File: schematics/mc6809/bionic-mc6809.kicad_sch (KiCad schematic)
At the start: 5 parts, among them J1 BionicConnector, U1 MC6809P, U2 74HCT126

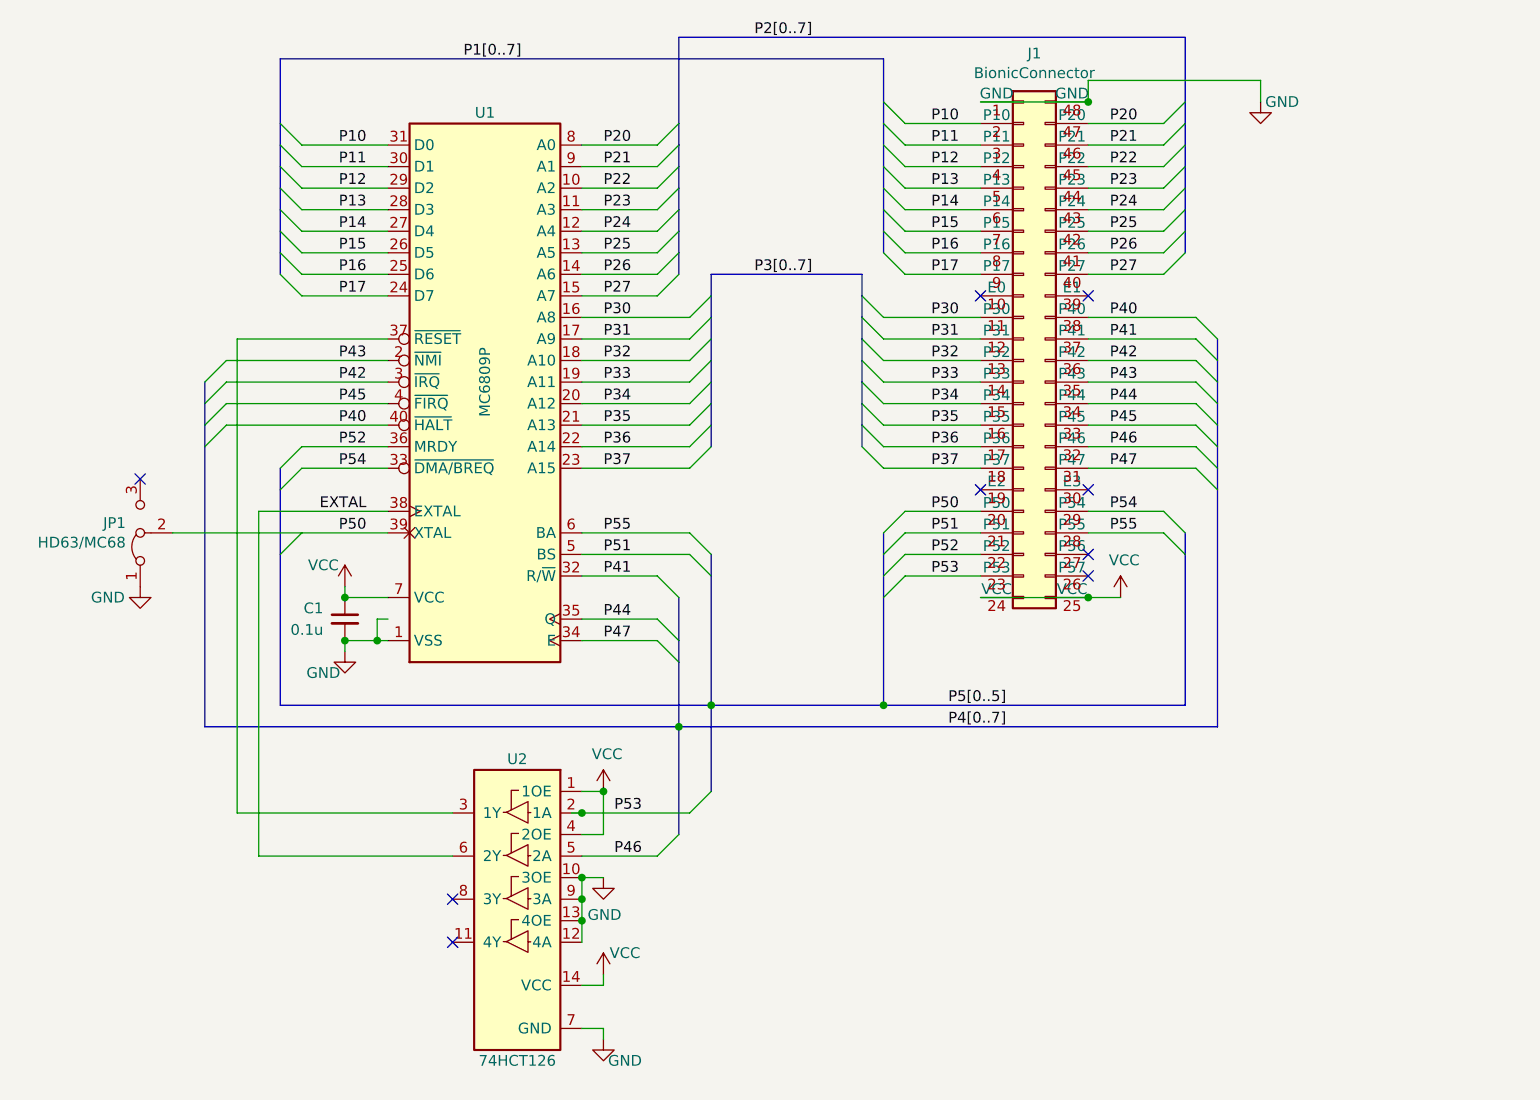
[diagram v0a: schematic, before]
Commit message: [MC6809] Move schematics directory
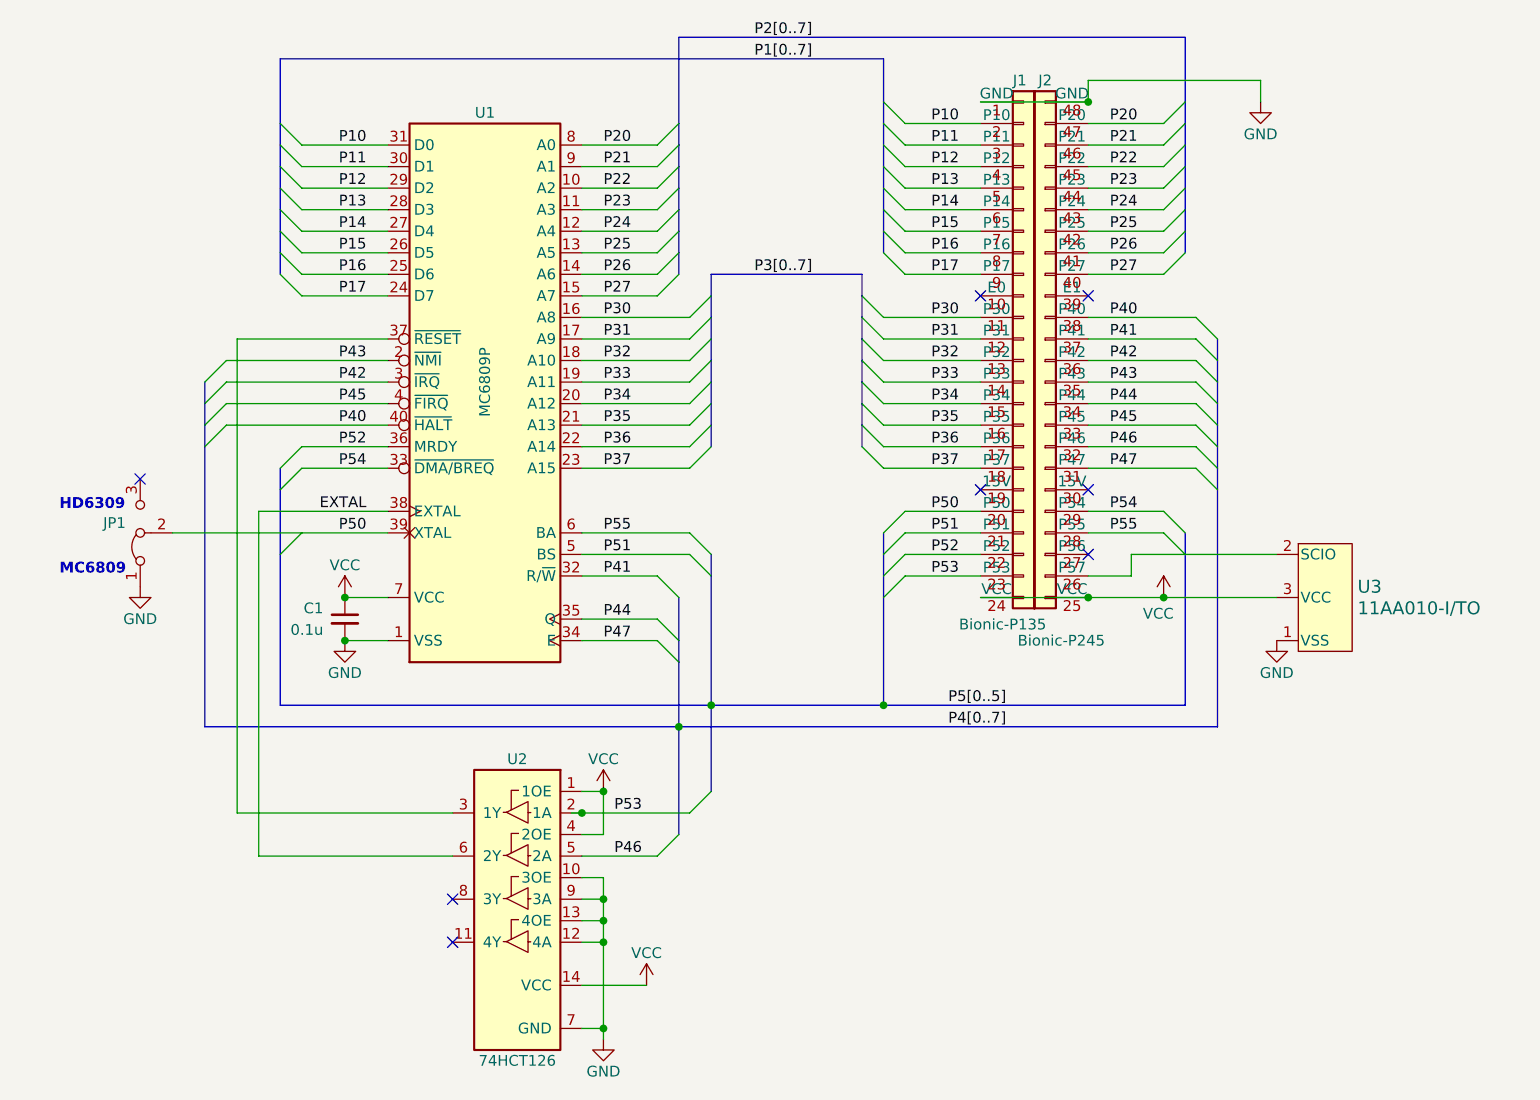
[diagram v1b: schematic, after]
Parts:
- removed J1: BionicConnector, 0-LocalLibrary:DIP-48_W7.62mm, symbol 0-LocalLibrary:BionicConnector
- added J1: Bionic-P135, connector:Bionic-P135_Vertical, symbol 0-LocalLibrary:Bionic-P135
- added J2: Bionic-P245, connector:Bionic-P245_Vertical, symbol 0-LocalLibrary:Bionic-P245
- added U3: 11AA010-I/TO, TO-92_MC_MCH, symbol 0-LocalLibrary:11AA010-I_TO
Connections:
- net GND: now also J1.1 (GND), J2.48 (GND), U3.1 (VSS)
- net P10: now also J1.2 (P10)
- net P11: now also J1.3 (P11)
- net P12: now also J1.4 (P12)
- net P13: now also J1.5 (P13)
- net P14: now also J1.6 (P14)
- net P15: now also J1.7 (P15)
- net P16: now also J1.8 (P16)
- net P17: now also J1.9 (P17)
- net P20: now also J2.47 (P20)
- net P21: now also J2.46 (P21)
- net P22: now also J2.45 (P22)
- net P23: now also J2.44 (P23)
- net P24: now also J2.43 (P24)
- net P25: now also J2.42 (P25)
- net P26: now also J2.41 (P26)
- net P27: now also J2.40 (P27)
- net P30: now also J1.11 (P30)
- net P31: now also J1.12 (P31)
- net P32: now also J1.13 (P32)
- net P33: now also J1.14 (P33)
- net P34: now also J1.15 (P34)
- net P35: now also J1.16 (P35)
- net P36: now also J1.17 (P36)
- net P37: now also J1.18 (P37)
- net P40: now also J2.38 (P40)
- net P41: now also J2.37 (P41)
- net P42: now also J2.36 (P42)
- net P43: now also J2.35 (P43)
- net P44: now also J2.34 (P44)
- net P45: now also J2.33 (P45)
- net P46: now also J2.32 (P46)
- net P47: now also J2.31 (P47)
- net P50: now also J1.20 (P50)
- net P51: now also J1.21 (P51)
- net P52: now also J1.22 (P52)
- net P53: now also J1.23 (P53)
- net P54: now also J2.29 (P54)
- net P55: now also J2.28 (P55)
- net VCC: now also J1.24 (VCC), J2.25 (VCC), U3.3 (VCC)
- new net: J2.26 (P57), U3.2 (SCIO)
- no-connect marks 9 -> 8
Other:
- note added: "HD6309"
- note added: "MC6809"
- title: BionicMC6809 Mezzanine -> BionicMC6809

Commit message: [MC6809] Remove HC126
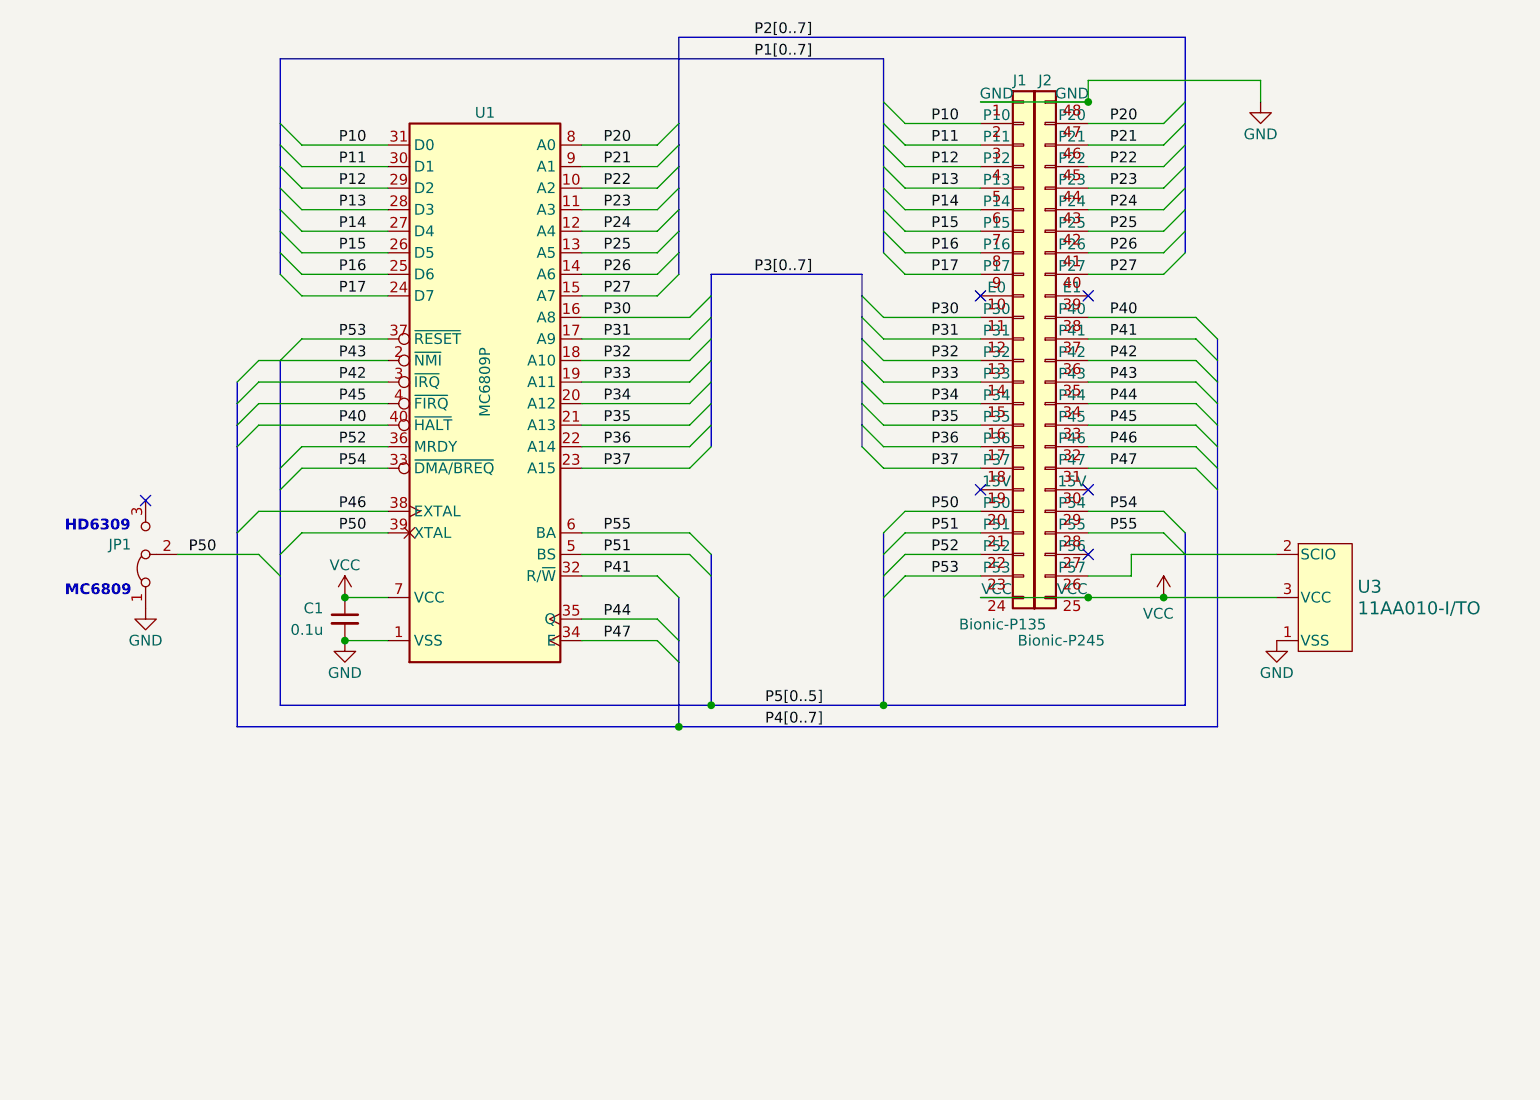
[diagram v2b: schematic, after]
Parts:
- removed U2: 74HCT126, Package_DIP:DIP-14_W7.62mm, symbol 0-LocalLibrary:74HCT126
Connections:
- net EXTAL is gone; now on net P46: U1.38 (EXTAL)
- net P53: now also U1.37 (~{RESET})
- no-connect marks 8 -> 6
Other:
- moved on the sheet: JP1
